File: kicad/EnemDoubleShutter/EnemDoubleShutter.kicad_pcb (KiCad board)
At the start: 2 copper layers, 90 x 90 mm, 11 parts

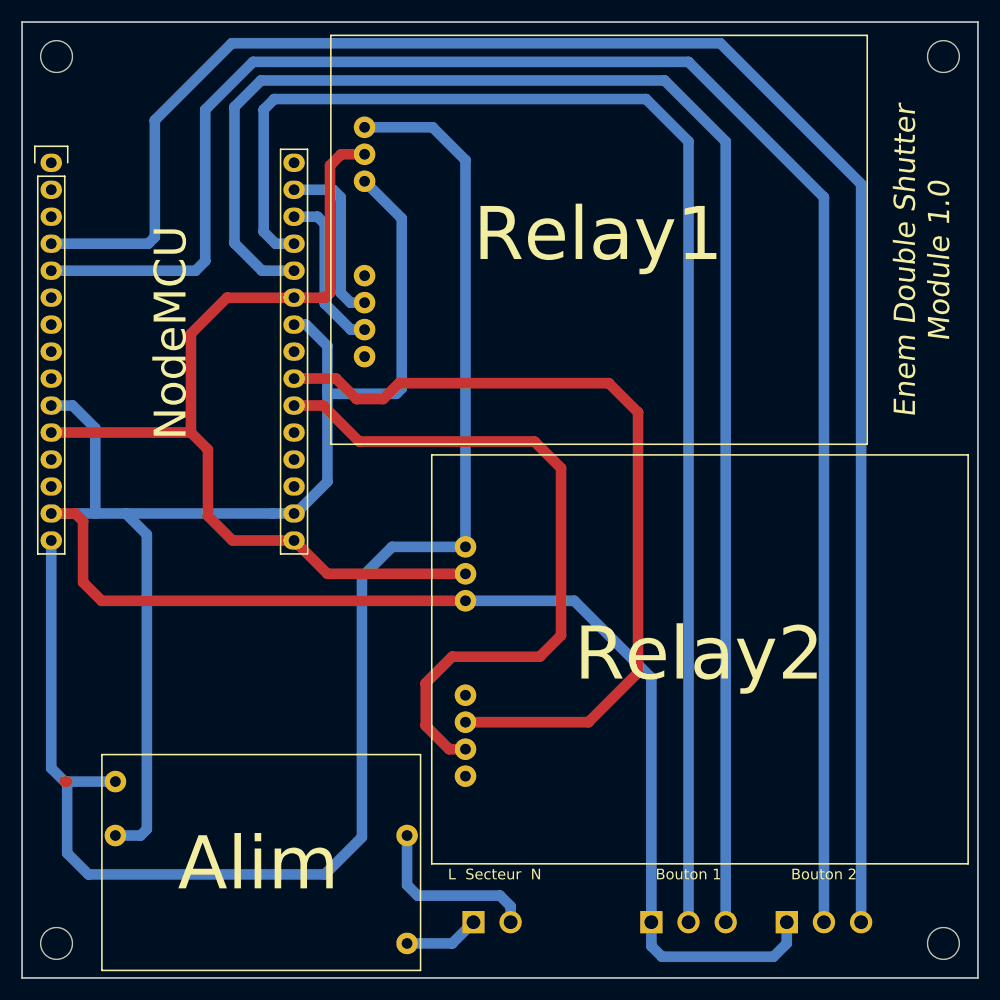
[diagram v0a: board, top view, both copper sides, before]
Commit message: Modifications légères sur les pistes. Ajout des noms des GPIO au niveau des boutons et déplacement du nom des boutons. Correction sur le commentaire arrière.
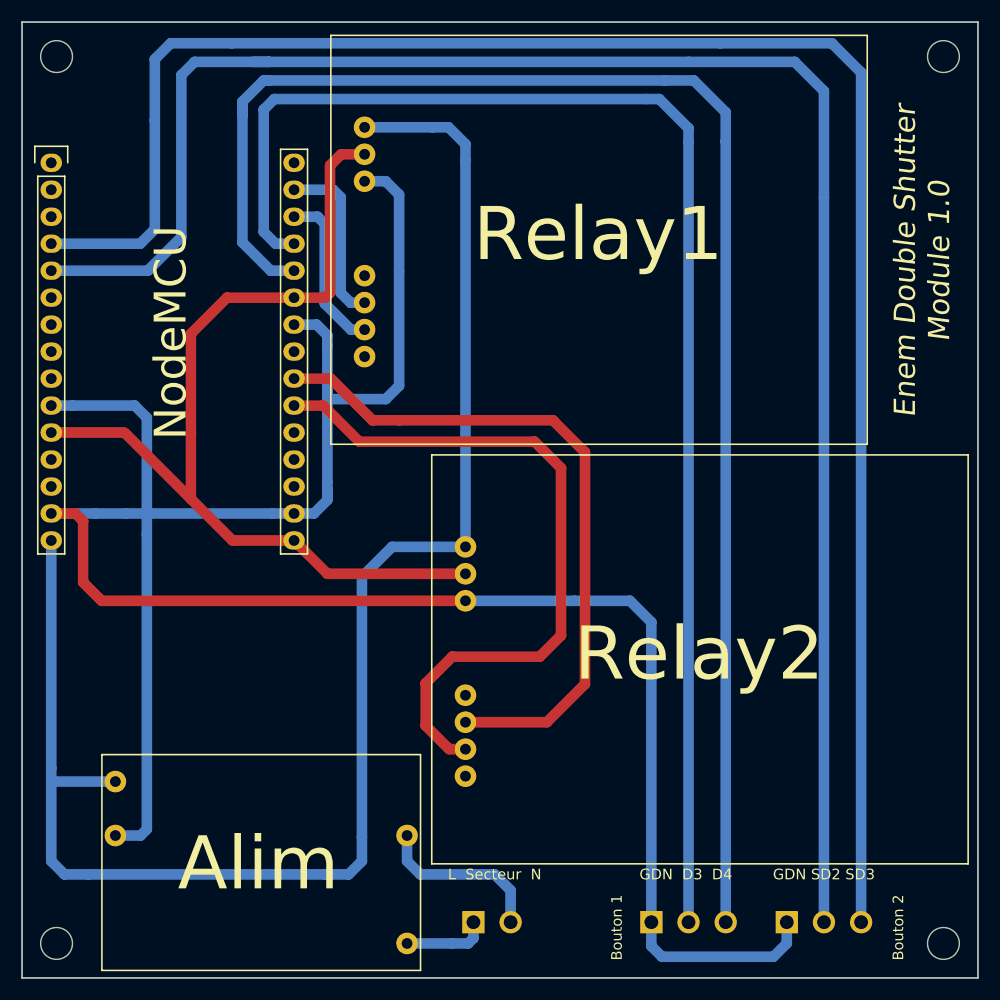
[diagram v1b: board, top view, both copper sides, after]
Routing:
- net Net-(Relay2-Pad4): track 77.6 -> 64.8 mm
- net GND: track 226.3 -> 237.7 mm
- net Net-(J3-Pad3): track 165.5 -> 174.6 mm
- net Net-(J3-Pad2): track 162.8 -> 170.7 mm
- net +5V: track 147.1 -> 152.8 mm
- net +3V3: track 87.8 -> 90.3 mm
- net Net-(J2-Pad3): track 142.7 -> 143.8 mm
- net Net-(A1-Pad1): track 7.08 -> 7.96 mm
- net Net-(J2-Pad2): track 130.4 -> 131.1 mm
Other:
- board text added: "Allez tous vous faire enculer par... Miou ! Bande d'enculés de merde qui font tous... chier ! Mosse et Poluu, deux abrutis de base qui cherchent à faire des bons trucs !"
- board text added: "GDN D3 D4"
- board text added: "GDN SD2 SD3"
- board text removed: "Allez tous vous faire enculer par... miou Bande d'enculés de merde qui font tous... chier Mosse et Poluu, deux abrutis de base qui cherchent à faire des bons trucs"

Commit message: Corrections et finalisation PCB
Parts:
- moved Bouton 1 12.8 mm to (117.0, 134.8)
- moved Bouton 2 12.8 mm to (104.2, 134.8)
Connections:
- NodeMCU pad 10: GND -> Net-(U1-Pad10)
- NodeMCU pad 11: +3V3 -> Net-(U1-Pad11)
- NodeMCU pad 16: +3V3 -> Net-(U1-Pad16)
- NodeMCU pad 20: Net-(U1-Pad20) -> Net-(J3-Pad3)
- NodeMCU pad 21: Net-(Relay2-Pad5) -> Net-(J3-Pad2)
- NodeMCU pad 22: Net-(Relay2-Pad4) -> Net-(Relay2-Pad5)
- NodeMCU pad 23: Net-(U1-Pad23) -> Net-(Relay2-Pad4)
- NodeMCU pad 4: Net-(J3-Pad3) -> Net-(U1-Pad4)
- NodeMCU pad 5: Net-(J3-Pad2) -> Net-(U1-Pad5)
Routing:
- net GND: track 237.7 -> 0.00 mm
- net Net-(J3-Pad2): track 170.7 -> 77.5 mm
- net Net-(J3-Pad3): track 174.6 -> 85.0 mm
- net Net-(J2-Pad3): track 143.8 -> 113.6 mm
- net Net-(J2-Pad2): track 131.1 -> 107.1 mm
- net +3V3: track 90.3 -> 73.6 mm
- net Net-(Relay2-Pad5): track 66.6 -> 52.3 mm
- net +5V: track 152.8 -> 144.1 mm
- net Net-(Relay2-Pad4): track 64.8 -> 73.5 mm
- net Net-(Relay1-Pad4): track 16.3 -> 20.6 mm
- net Net-(A1-Pad2): track 16.3 -> 14.0 mm
- net Net-(Relay1-Pad5): track 15.4 -> 16.6 mm
- net Net-(A1-Pad1): track 7.96 -> 7.08 mm
- added copper zone on B.Cu, net GND
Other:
- board text added: "Allez tous vous faire enculer par... Miou ! Bande d'enculés de merde qui font tous... chier ! Mosse et Poluu, deux abrutis de base qui cherchent à faire des bons trucs ! C'est un hommage pour vous le crapaud roteur !"
- board text added: "GND UP DOWN"
- board text removed: "Allez tous vous faire enculer par... Miou ! Bande d'enculés de merde qui font tous... chier ! Mosse et Poluu, deux abrutis de base qui cherchent à faire des bons trucs !"
- board text removed: "GDN D3 D4"
- board text removed: "GDN SD2 SD3"
